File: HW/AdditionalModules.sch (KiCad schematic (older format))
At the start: 14 parts, among them U40 AT_CryptoAuth

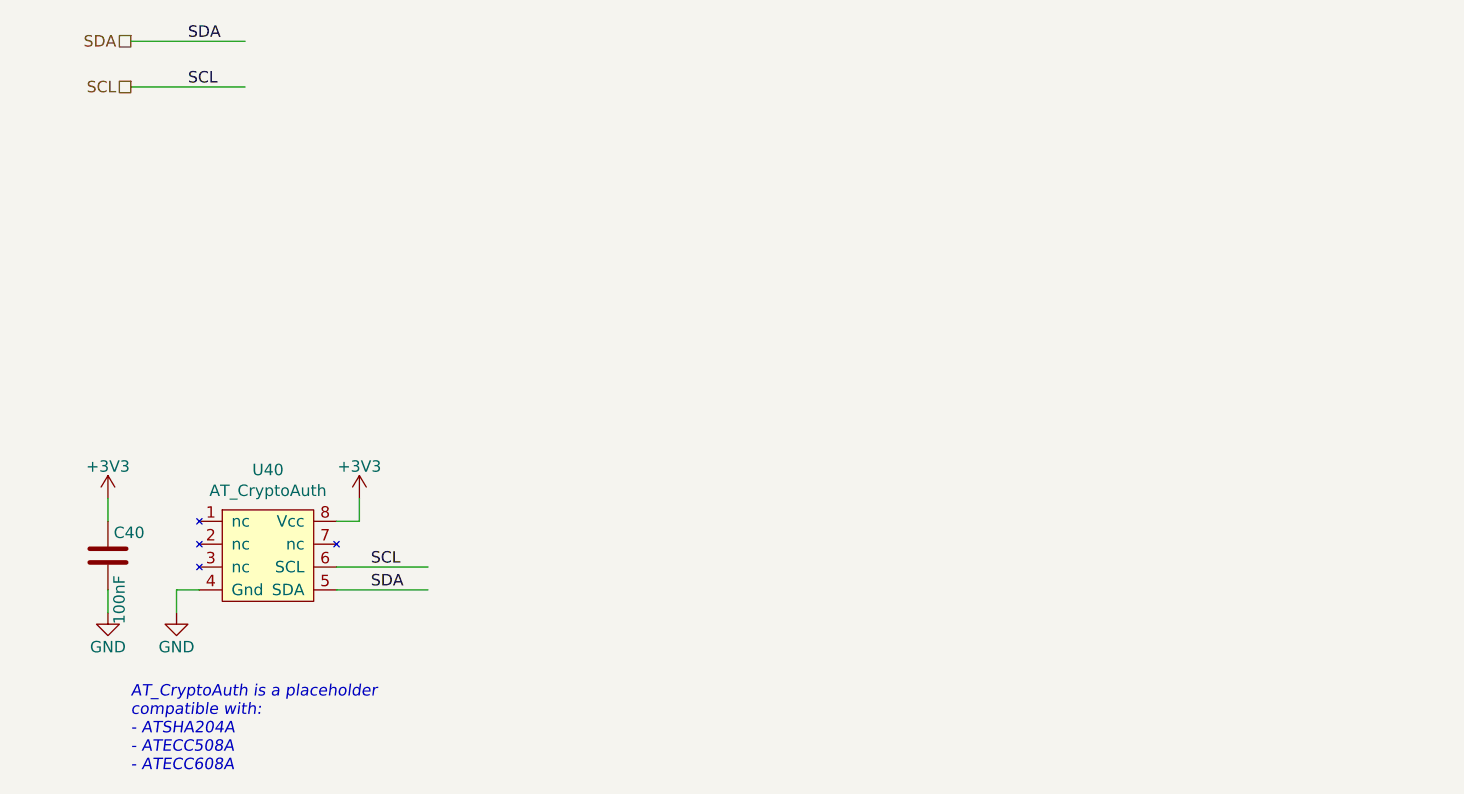
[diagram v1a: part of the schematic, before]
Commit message: Adds DTR and RTS connector and the components for automatic setting of EN and Boot signals
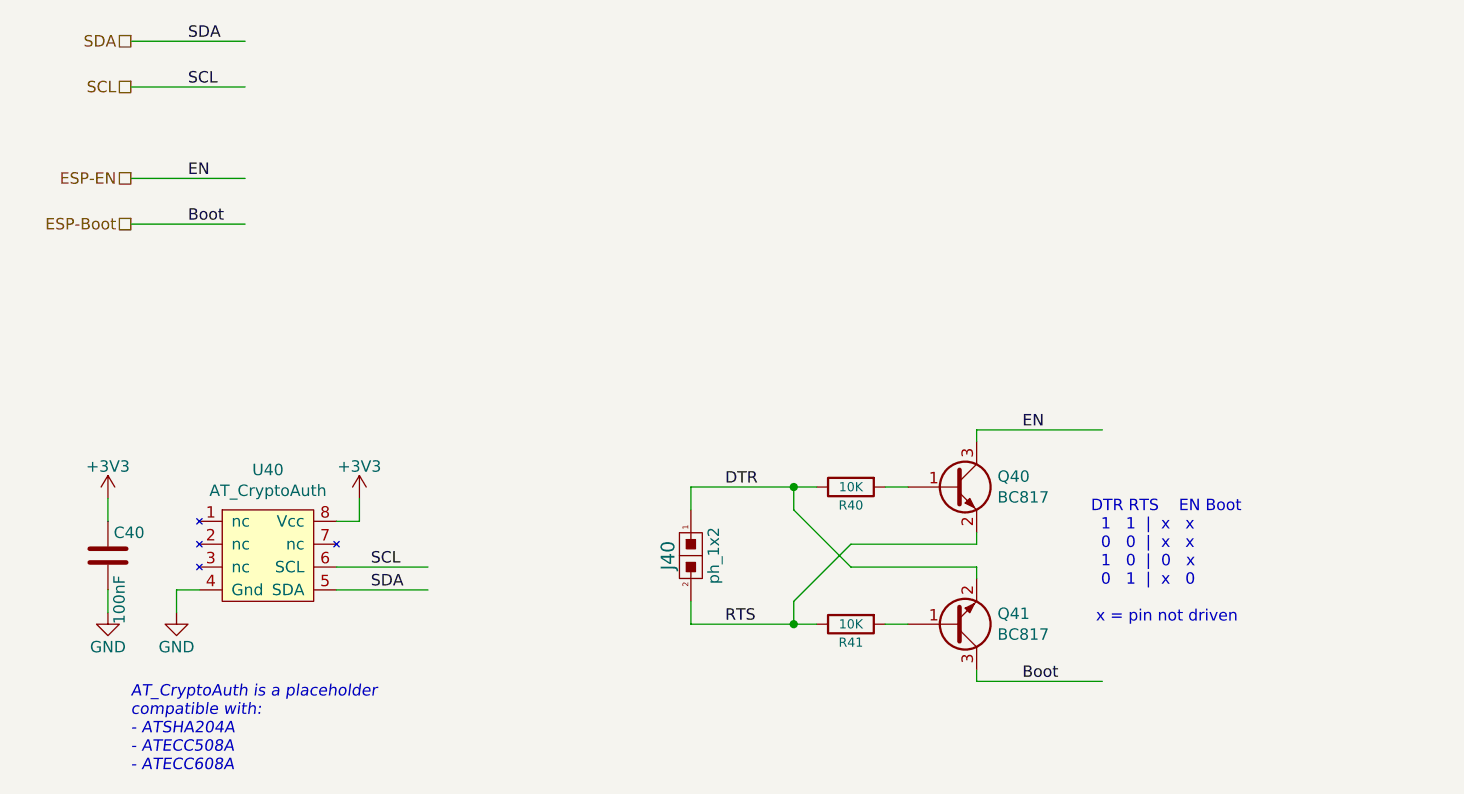
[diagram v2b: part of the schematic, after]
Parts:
- added J40: ph_1x2, CalinConnectors:Pin_Header_Straight_1x02, symbol calin:CS_2
- added Q40, Q41: BC817, CalinGeneric:SOT-23, symbol Transistor_BJT:BC817
- added R40, R41: 10K, CalinGeneric:R0805HS, symbol calin:R
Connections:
- net labels added: Boot, DTR, EN, ESP-Boot, ESP-EN, RTS
- wire segments 22 -> 44
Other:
- note added: "DTR RTS EN Boot\n 1 1 | x x\n 0 0 | x x\n 1 0 | 0 x\n 0 1 | x 0\n\n x = pin not driven"
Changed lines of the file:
@@
 Title "ESP32 RFM69/RFM9x Gateway"
 Date "2019-04-22"
-Rev "27"
+Rev "28"
 Comp "Calin Radoni"
 Comment1 ""
@@
 NoConn ~ 7900 1800
 NoConn ~ 7900 2100
+$Comp
+L calin:CS_2 J40
+U 1 1 5CC0953E
+P 3950 3450
+F 0 "J40" V 3850 3450 60  0000 C CNN
+F 1 "ph_1x2" V 4050 3450 50  0000 C CNN
+F 2 "CalinConnectors:Pin_Header_Straight_1x02" H 3950 3500 60  0001 C CNN
+F 3 "" H 3950 3500 60  0000 C CNN
+	1    3950 3450
+	1    0    0    -1
+$EndComp
+$Comp
+L calin:R R?
+U 1 1 5CC095F4
+P 4650 3150
+AR Path="/5CC095F4" Ref="R?"  Part="1"
+AR Path="/5CCB086C/5CC095F4" Ref="R40"  Part="1"
+F 0 "R40" V 4730 3150 40  0000 C CNN
+F 1 "10K" V 4650 3150 40  0000 C CNN
+F 2 "CalinGeneric:R0805HS" V 4580 3150 30  0001 C CNN
+F 3 "" H 4650 3150 30  0000 C CNN
+	1    4650 3150
+	0    1    1    0
+$EndComp
+$Comp
+L calin:R R?
+U 1 1 5CC096FF
+P 4650 3750
+AR Path="/5CC096FF" Ref="R?"  Part="1"
+AR Path="/5CCB086C/5CC096FF" Ref="R41"  Part="1"
+F 0 "R41" V 4730 3750 40  0000 C CNN
+F 1 "10K" V 4650 3750 40  0000 C CNN
+F 2 "CalinGeneric:R0805HS" V 4580 3750 30  0001 C CNN
+F 3 "" H 4650 3750 30  0000 C CNN
+	1    4650 3750
+	0    1    1    0
+$EndComp
+$Comp
+L Transistor_BJT:BC817 Q40
+U 1 1 5CC09CBF
+P 5100 3150
+F 0 "Q40" H 5291 3196 50  0000 L CNN
+F 1 "BC817" H 5291 3105 50  0000 L CNN
+F 2 "CalinGeneric:SOT-23" H 5300 3075 50  0001 L CIN
+F 3 "http://www.fairchildsemi.com/ds/BC/BC817.pdf" H 5100 3150 50  0001 L CNN
+	1    5100 3150
+	1    0    0    -1
+$EndComp
+$Comp
+L Transistor_BJT:BC817 Q41
+U 1 1 5CC09D1F
+P 5100 3750
+F 0 "Q41" H 5291 3704 50  0000 L CNN
+F 1 "BC817" H 5291 3795 50  0000 L CNN
+F 2 "CalinGeneric:SOT-23" H 5300 3675 50  0001 L CIN
+F 3 "http://www.fairchildsemi.com/ds/BC/BC817.pdf" H 5100 3750 50  0001 L CNN
+	1    5100 3750
+	1    0    0    1
+$EndComp
+Wire Wire Line
+	4900 3150 4800 3150
+Wire Wire Line
+	4900 3750 4800 3750
+Wire Wire Line
+	4500 3150 4400 3150
+Wire Wire Line
+	3950 3150 3950 3250
+Wire Wire Line
+	4500 3750 4400 3750
+Wire Wire Line
+	3950 3750 3950 3650
+Wire Wire Line
+	5200 3550 5200 3500
+Wire Wire Line
+	5200 3500 4650 3500
+Wire Wire Line
+	4650 3500 4400 3250
+Wire Wire Line
+	4400 3250 4400 3150
+Connection ~ 4400 3150
+Wire Wire Line
+	4400 3150 3950 3150
+Wire Wire Line
+	5200 3350 5200 3400
+Wire Wire Line
+	5200 3400 4650 3400
+Wire Wire Line
+	4650 3400 4400 3650
+Wire Wire Line
+	4400 3650 4400 3750
+Connection ~ 4400 3750
+Wire Wire Line
+	4400 3750 3950 3750
+Text Label 4100 3150 0    50   ~ 0
+DTR
+Text Label 4100 3750 0    50   ~ 0
+RTS
+Wire Wire Line
+	5200 2950 5200 2900
+Wire Wire Line
+	5200 2900 5750 2900
+Wire Wire Line
+	5200 3950 5200 4000
+Wire Wire Line
+	5200 4000 5750 4000
+Text Label 5400 2900 0    50   ~ 0
+EN
+Text Label 5400 4000 0    50   ~ 0
+Boot
+Text Notes 5700 3750 0    50   ~ 0
+DTR RTS    EN Boot\n  1   1  |  x   x\n  0   0  |  x   x\n  1   0  |  0   x\n  0   1  |  x   0\n\n x = pin not driven
+Text HLabel 1500 1800 0    50   UnSpc ~ 0
+ESP-EN
+Text HLabel 1500 2000 0    50   UnSpc ~ 0
+ESP-Boot
+Wire Wire Line
+	1500 1800 2000 1800
+Wire Wire Line
+	1500 2000 2000 2000
+Text Label 1750 1800 0    50   ~ 0
+EN
+Text Label 1750 2000 0    50   ~ 0
+Boot
 $EndSCHEMATC

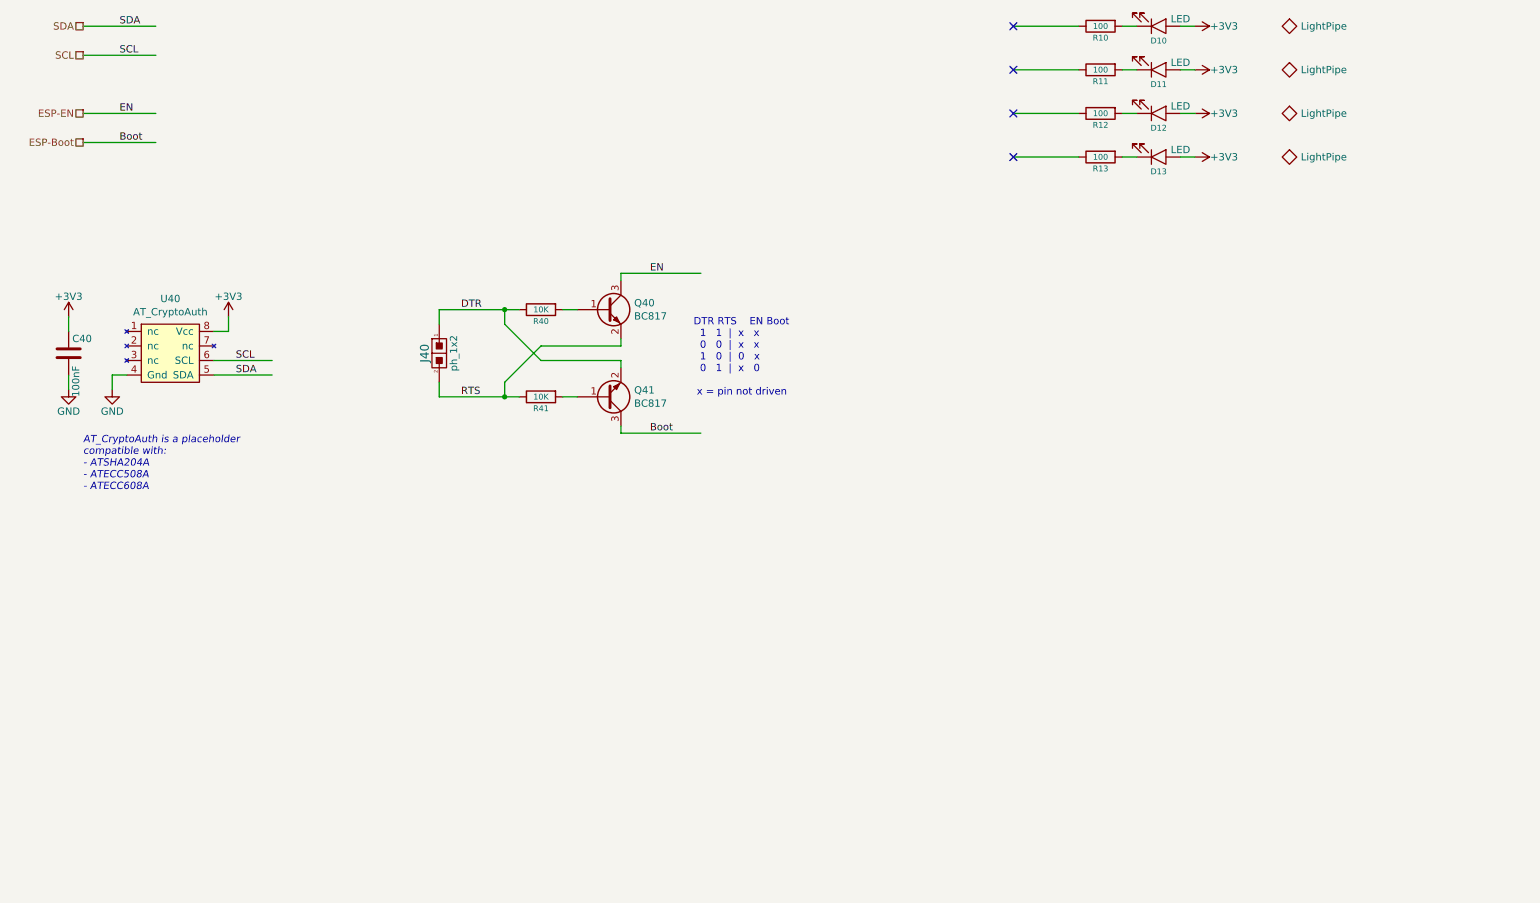
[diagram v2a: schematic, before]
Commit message: Adds the I2C LED driver and more track tunning
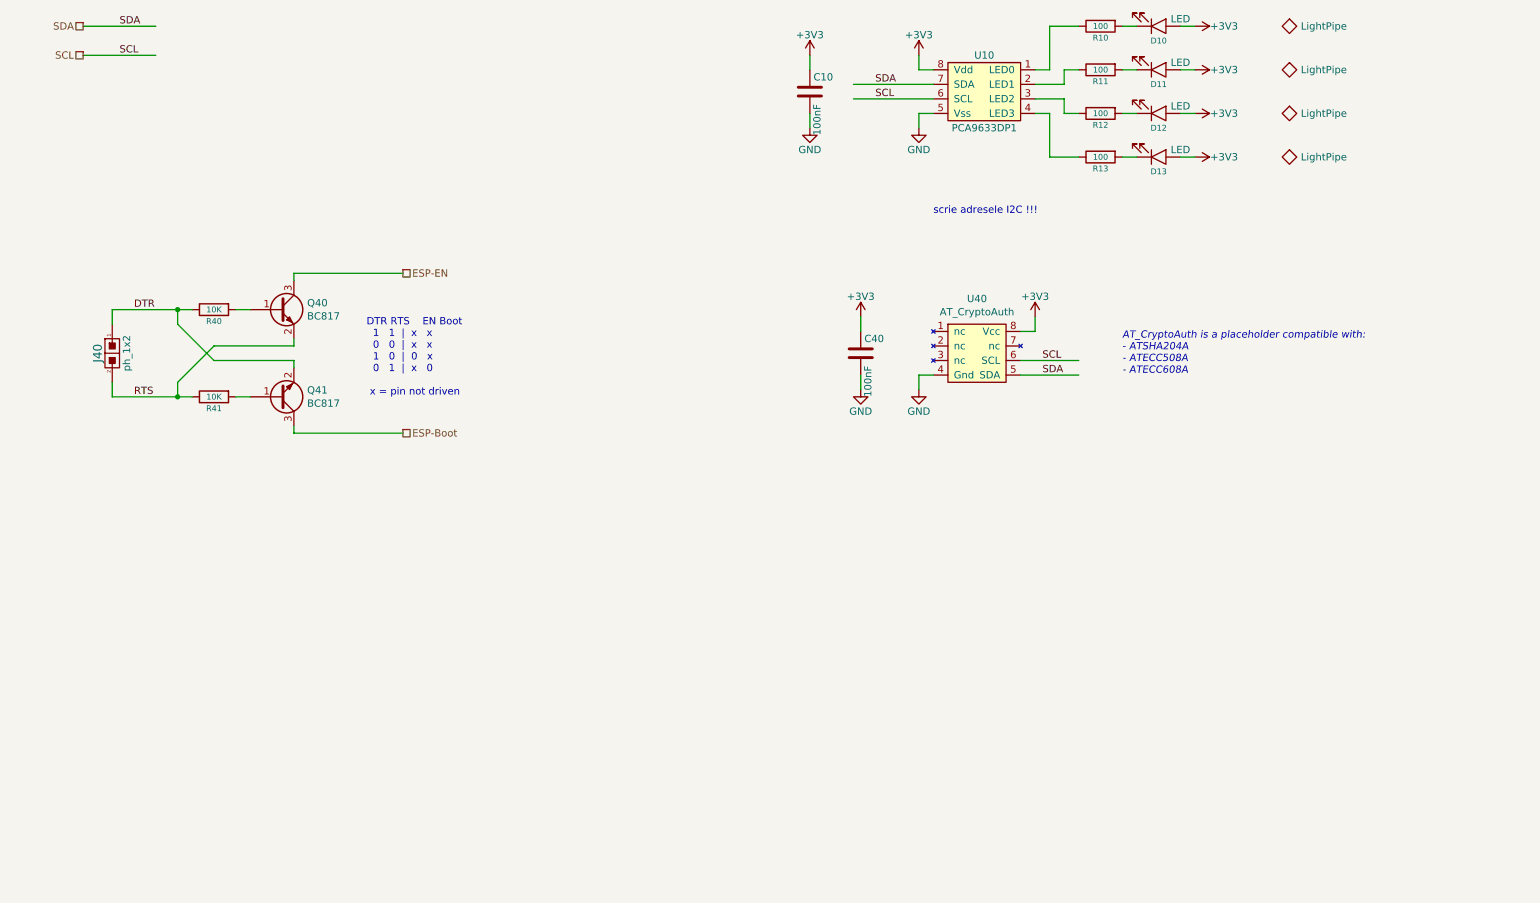
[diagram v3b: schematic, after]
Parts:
- added C10: 100nF, CalinGeneric:C0805HS, symbol Device:C
- added U10: PCA9633DP1, CalinGeneric:TSSOP8-SOT505-1-HS, symbol calin:PCA9633DP1
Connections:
- net labels removed: Boot, EN
- wire segments 44 -> 58
- no-connect marks 4 -> 0
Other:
- note added: "AT_CryptoAuth is a placeholder compatible with:\n- ATSHA204A\n- ATECC508A\n- ATECC608A"
- note added: "scrie adresele I2C !!!"
- note removed: "AT_CryptoAuth is a placeholder\ncompatible with:\n- ATSHA204A\n- ATECC508A\n- ATECC608A"
- moved on the sheet: C40, J40, Q40, Q41, R40, R41, U40

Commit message: Adds the HIH8xxx humidity and temperature sensor
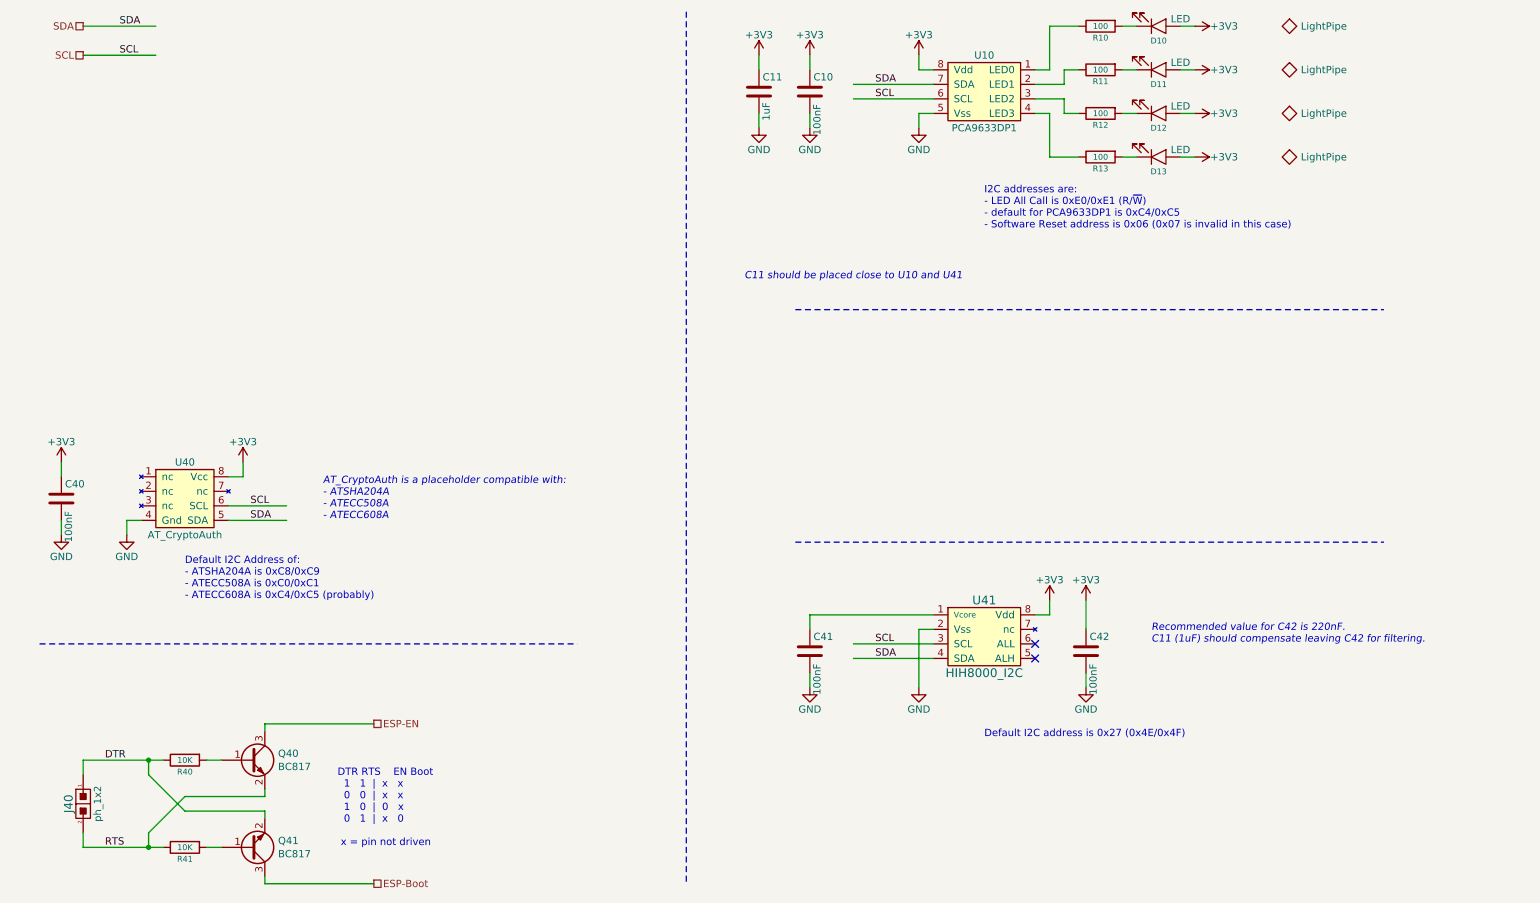
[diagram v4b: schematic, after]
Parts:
- added C11: 1uF, CalinGeneric:C0805HS, symbol Device:C
- added C41, C42: 100nF, CalinGeneric:C0805HS, symbol Device:C
- added U41: HIH8000_I2C, CalinGeneric:SOIC-8-HS, symbol calin:HIH8000_I2C
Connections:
- wire segments 58 -> 71
- no-connect marks 0 -> 2
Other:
- note added: "C11 should be placed close to U10 and U41"
- note added: "Default I2C Address of:\n- ATSHA204A is 0xC8/0xC9\n- ATECC508A is 0xC0/0xC1\n- ATECC608A is 0xC4/0xC5 (probably)"
- note added: "Default I2C address is 0x27 (0x4E/0x4F)"
- note added: "I2C addresses are:\n- LED All Call is 0xE0/0xE1 (R/~W)\n- default for PCA9633DP1 is 0xC4/0xC5\n- Software Reset address is 0x06 (0x07 is invalid in this case)"
- note added: "Recommended value for C42 is 220nF.\nC11 (1uF) should compensate leaving C42 for filtering."
- note removed: "scrie adresele I2C !!!"
- moved on the sheet: C40, J40, Q40, Q41, R40, R41, U40
